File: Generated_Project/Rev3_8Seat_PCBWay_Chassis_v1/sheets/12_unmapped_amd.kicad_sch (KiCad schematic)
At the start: 0 parts

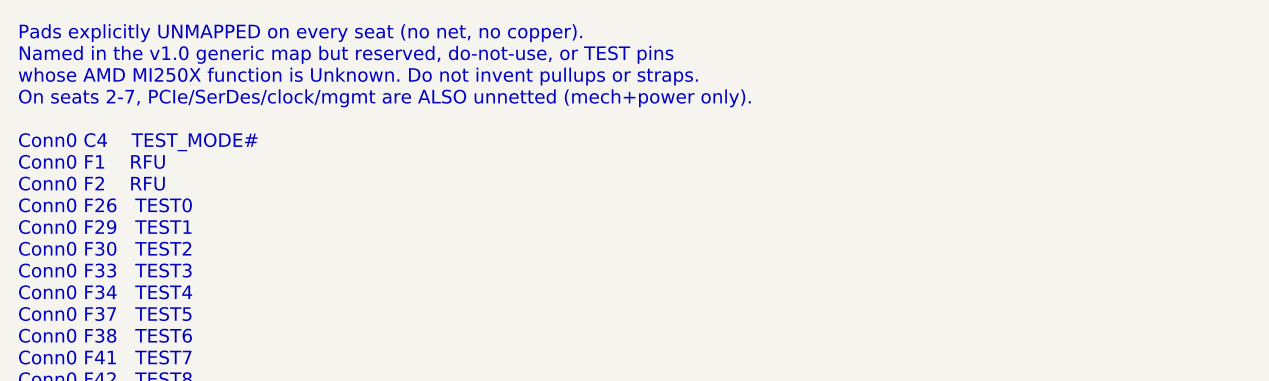
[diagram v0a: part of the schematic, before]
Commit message: Raise Rev3 chassis to 8 electrically designed seats.
Name v1.0 power/PE/clock nets on all eight OAM seats toward two DNP
PM8536B-FEI (x8 per GCD), keep SB175 star + local P48V pours, and generate
the 12-layer 2.0 mm stuffed-switch target. First stuffing may still populate
two modules; the PCB does not need a respin for the other six.

Do not fabricate. Do not energize P48V.

Co-authored-by: zivzancoeli-commits <zivzancoeli-commits@users.noreply.github.com>
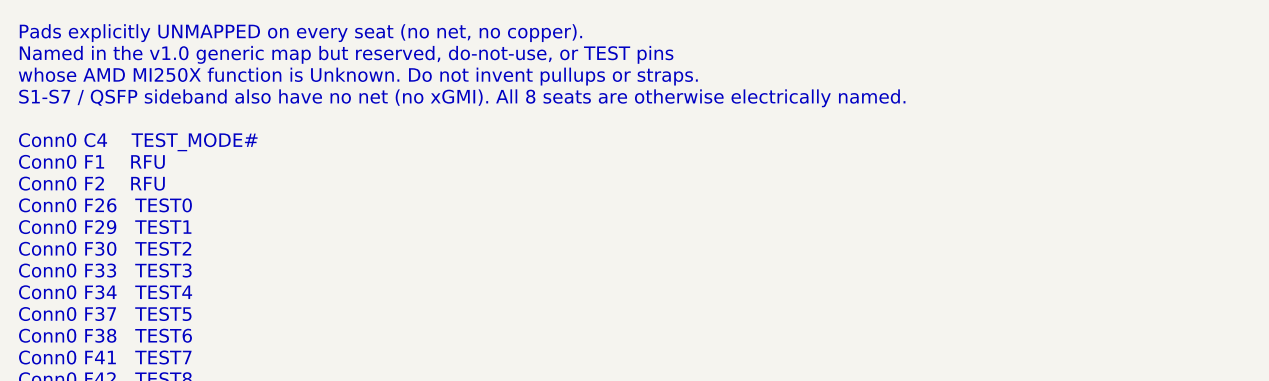
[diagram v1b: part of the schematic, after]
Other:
- note added: "Pads explicitly UNMAPPED on every seat (no net, no copper). Named in the v1.0 generic map but reserved, do-not-use, or TEST pins whose AMD MI250X function is Unknown. Do not invent pullups or straps. S1-S7 / QSFP sideband also have no net (no xGMI). All 8 seats are otherwise electrically named. Conn0 C4 TEST_MODE# Conn0 F1 RFU Conn0 F2 RFU Conn0 F26 TEST0 Conn0 F29 TEST1 Conn0 F30 TEST2 Conn0 F33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"
- note removed: "Pads explicitly UNMAPPED on every seat (no net, no copper). Named in the v1.0 generic map but reserved, do-not-use, or TEST pins whose AMD MI250X function is Unknown. Do not invent pullups or straps. On seats 2-7, PCIe/SerDes/clock/mgmt are ALSO unnetted (mech+power only). Conn0 C4 TEST_MODE# Conn0 F1 RFU Conn0 F2 RFU Conn0 F26 TEST0 Conn0 F29 TEST1 Conn0 F30 TEST2 Conn0 F33 TEST3 Conn0 F34 TEST4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"
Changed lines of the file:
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@@
 		(date "2026-08-21")
 		(rev "Rev3_8Seat_PCBWay_v1")
-		(comment 1 "DO NOT FABRICATE. DO NOT ENERGIZE P48V. Ticket 167157 open.")
-		(comment 2 "Documentation sheet — no invented nets")
-		(comment 3 "Pin names: OAM Pin map rev 1.0.xlsx — OCP generic, NOT AMD overlay")
-		(comment 4 "r2.0 maps UNUSABLE. P3V3=2 Conn0 C1/C2. 8-seat PCBWay chassis stub.")
+        (comment 1 "DO NOT FABRICATE. DO NOT ENERGIZE P48V. Molex 60V written 2026-08-18; 1.2A/contact OPEN.")
+        (comment 2 "Documentation sheet — no invented nets")
+        (comment 3 "Pin names: OAM Pin map rev 1.0.xlsx — OCP generic, NOT AMD overlay")
+        (comment 4 "r2.0 UNUSABLE. P3V3=Conn0 C1/C2. 12L 2.0mm stuffed-switch TARGET. Star-fed P48V.")
 	)
-	(text "Pads explicitly UNMAPPED on every seat (no net, no copper).\nNamed in the v1.0 generic map but reserved, do-not-use, or TEST pins\nwhose AMD MI250X function is Unknown. Do not invent pullups or straps.\nOn seats 2-7, PCIe/SerDes/clock/mgmt are ALSO unnetted (mech+power only).\n\nConn0 C4    TEST_MODE#\nConn0 F1    RFU\nConn0 F2    RFU\nConn0 F26   TEST0\nConn0 F29   TEST1\nConn0 F30   TEST2\nConn0 F33   TEST3\nConn0 F34   TEST4\nConn0 F37   TEST5\nConn0 F38   TEST6\nConn0 F41   TEST7\nConn0 F42   TEST8\nConn0 F49   TEST9\nConn0 F5    RFU\nConn0 F50   RFU\nConn0 H58   DO_NOT_USE\nConn0 J60   DO_NOT_USE\nConn0 K58   DO_NOT_USE\nConn0 L60   DO_NOT_USE\nConn1 A7    RFU\nConn1 A8    RFU\nConn1 B5    RFU\nConn1 B6    RFU\nConn1 C3    RFU\nConn1 C4    RFU\nConn1 C59   RFU\nConn1 C60   RFU\nConn1 C7    RFU\nConn1 C8    RFU\nConn1 E31   RFU\nConn1 E32   RFU\nConn1 E39   RFU\nConn1 E40   RFU\nConn1 F13   TEST10\nConn1 F14   TEST11\nConn1 F17   TEST12\nConn1 F18   TEST13\nConn1 F21   TEST14\nConn1 F22   RFU\nConn1 F29   RFU\nConn1 F30   RFU\nConn1 F33   RFU\nConn1 F34   RFU\nConn1 F37   RFU\nConn1 F38   RFU\nConn1 F41   RFU\nConn1 F42   RFU\nConn1 F45   RFU\nConn1 G3    RFU\nConn1 G31   RFU\nConn1 G32   RFU\nConn1 G4    RFU\nConn1 G7    RFU\nConn1 G8    RFU\nConn1 H5    RFU\nConn1 H6    RFU\nConn1 J3    RFU\nConn1 J4    RFU\nConn1 J64   RFU"
+	(text "Pads explicitly UNMAPPED on every seat (no net, no copper).\nNamed in the v1.0 generic map but reserved, do-not-use, or TEST pins\nwhose AMD MI250X function is Unknown. Do not invent pullups or straps.\nS1-S7 / QSFP sideband also have no net (no xGMI). All 8 seats are otherwise electrically named.\n\nConn0 C4    TEST_MODE#\nConn0 F1    RFU\nConn0 F2    RFU\nConn0 F26   TEST0\nConn0 F29   TEST1\nConn0 F30   TEST2\nConn0 F33   TEST3\nConn0 F34   TEST4\nConn0 F37   TEST5\nConn0 F38   TEST6\nConn0 F41   TEST7\nConn0 F42   TEST8\nConn0 F49   TEST9\nConn0 F5    RFU\nConn0 F50   RFU\nConn0 H58   DO_NOT_USE\nConn0 J60   DO_NOT_USE\nConn0 K58   DO_NOT_USE\nConn0 L60   DO_NOT_USE\nConn1 A7    RFU\nConn1 A8    RFU\nConn1 B5    RFU\nConn1 B6    RFU\nConn1 C3    RFU\nConn1 C4    RFU\nConn1 C59   RFU\nConn1 C60   RFU\nConn1 C7    RFU\nConn1 C8    RFU\nConn1 E31   RFU\nConn1 E32   RFU\nConn1 E39   RFU\nConn1 E40   RFU\nConn1 F13   TEST10\nConn1 F14   TEST11\nConn1 F17   TEST12\nConn1 F18   TEST13\nConn1 F21   TEST14\nConn1 F22   RFU\nConn1 F29   RFU\nConn1 F30   RFU\nConn1 F33   RFU\nConn1 F34   RFU\nConn1 F37   RFU\nConn1 F38   RFU\nConn1 F41   RFU\nConn1 F42   RFU\nConn1 F45   RFU\nConn1 G3    RFU\nConn1 G31   RFU\nConn1 G32   RFU\nConn1 G4    RFU\nConn1 G7    RFU\nConn1 G8    RFU\nConn1 H5    RFU\nConn1 H6    RFU\nConn1 J3    RFU\nConn1 J4    RFU\nConn1 J64   RFU"
 		(exclude_from_sim no)
 		(at 20.32 20.32 0)
